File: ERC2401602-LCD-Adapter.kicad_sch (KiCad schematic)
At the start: 27 parts, among them J1 LCD ERC240160XX-2, J2 Backlight, J3 LCD Debug, J4 Backlight Debug, J5 Left, J6 Bottom, Q1 2N7002

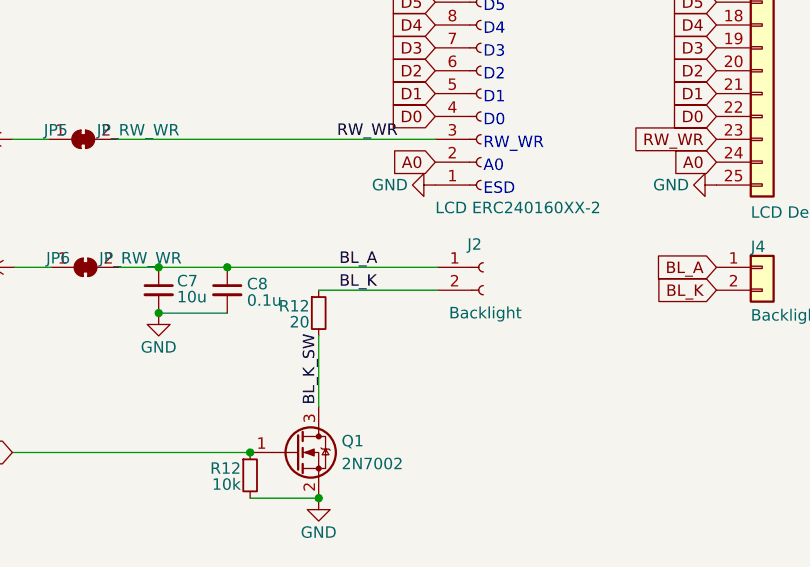
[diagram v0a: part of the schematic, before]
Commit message: Fixed Resistor and BG Polarity
- Changed the current limiting resistor value to 3.9R
- Fixed the Background Light connector Polarity
- Moved the LCD connector down 5mm
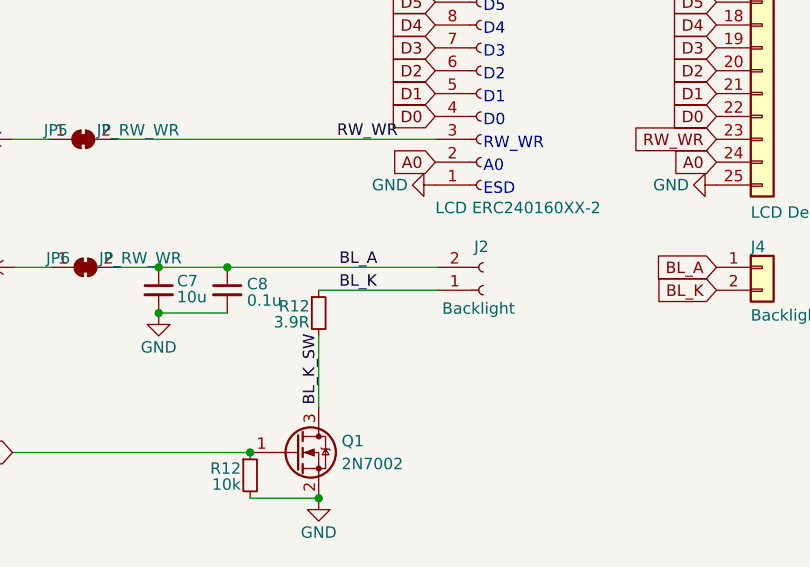
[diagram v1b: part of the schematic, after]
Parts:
- R12: value 20 -> 3.9R; LCSC (none) -> C2907146
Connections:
- net BL_A: now also J2.2 (Pin_2); no longer J2.1 (Pin_1)
- net BL_K: now also J2.1 (Pin_1); no longer J2.2 (Pin_2)
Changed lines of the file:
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@@
       (effects (font (size 1.27 1.27)) (justify right))
     )
-    (property "Value" "20" (at 212.852 106.426 0)
+    (property "Value" "3.9R" (at 212.852 106.426 0)
       (effects (font (size 1.27 1.27)) (justify right))
     )
@@
       (effects (font (size 1.27 1.27)) hide)
     )
-    (property "LCSC" "" (at 213.868 105.41 0)
-      (effects (font (size 1.27 1.27)) hide)
-    )
-    (property "Field5" "" (at 213.868 105.41 0)
+    (property "LCSC" "C2907146" (at 213.868 105.41 0)
       (effects (font (size 1.27 1.27)) hide)
     )
@@
     )
   )
-  (symbol (lib_id "Connector:Conn_01x02_Socket") (at 232.156 100.33 0) (unit 1)
-    (in_bom yes) (on_board yes) (dnp no)
-    (property "Reference" "J2" (at 230.378 97.79 0)
-      (effects (font (size 1.27 1.27)) (justify left))
-    )
-    (property "Value" "Backlight" (at 228.346 105.41 0)
-      (effects (font (size 1.27 1.27)) (justify left))
-    )
-    (property "Footprint" "Connector_JST:JST_PH_S2B-PH-SM4-TB_1x02-1MP_P2.00mm_Horizontal" (at 232.156 100.33 0)
-      (effects (font (size 1.27 1.27)) hide)
-    )
-    (property "Datasheet" "https://jlcpcb.com/partdetail/Jst-S2B_PH_SM4_TB_LF_SN/C295747" (at 232.156 100.33 0)
-      (effects (font (size 1.27 1.27)) hide)
-    )
-    (property "LCSC" "C295747" (at 232.156 100.33 0)
-      (effects (font (size 1.27 1.27)) hide)
-    )
+  (symbol (lib_id "Connector:Conn_01x02_Socket") (at 232.156 102.87 0) (mirror x) (unit 1)
+    (in_bom yes) (on_board yes) (dnp no)
+    (property "Reference" "J2" (at 231.14 98.044 0)
+      (effects (font (size 1.27 1.27)) (justify left))
+    )
+    (property "Value" "Backlight" (at 227.584 104.902 0)
+      (effects (font (size 1.27 1.27)) (justify left))
+    )
+    (property "Footprint" "Connector_JST:JST_PH_S2B-PH-SM4-TB_1x02-1MP_P2.00mm_Horizontal" (at 232.156 102.87 0)
+      (effects (font (size 1.27 1.27)) hide)
+    )
+    (property "Datasheet" "https://jlcpcb.com/partdetail/Jst-S2B_PH_SM4_TB_LF_SN/C295747" (at 232.156 102.87 0)
+      (effects (font (size 1.27 1.27)) hide)
+    )
+    (property "LCSC" "C295747" (at 232.156 102.87 0)
+      (effects (font (size 1.27 1.27)) hide)
+    )

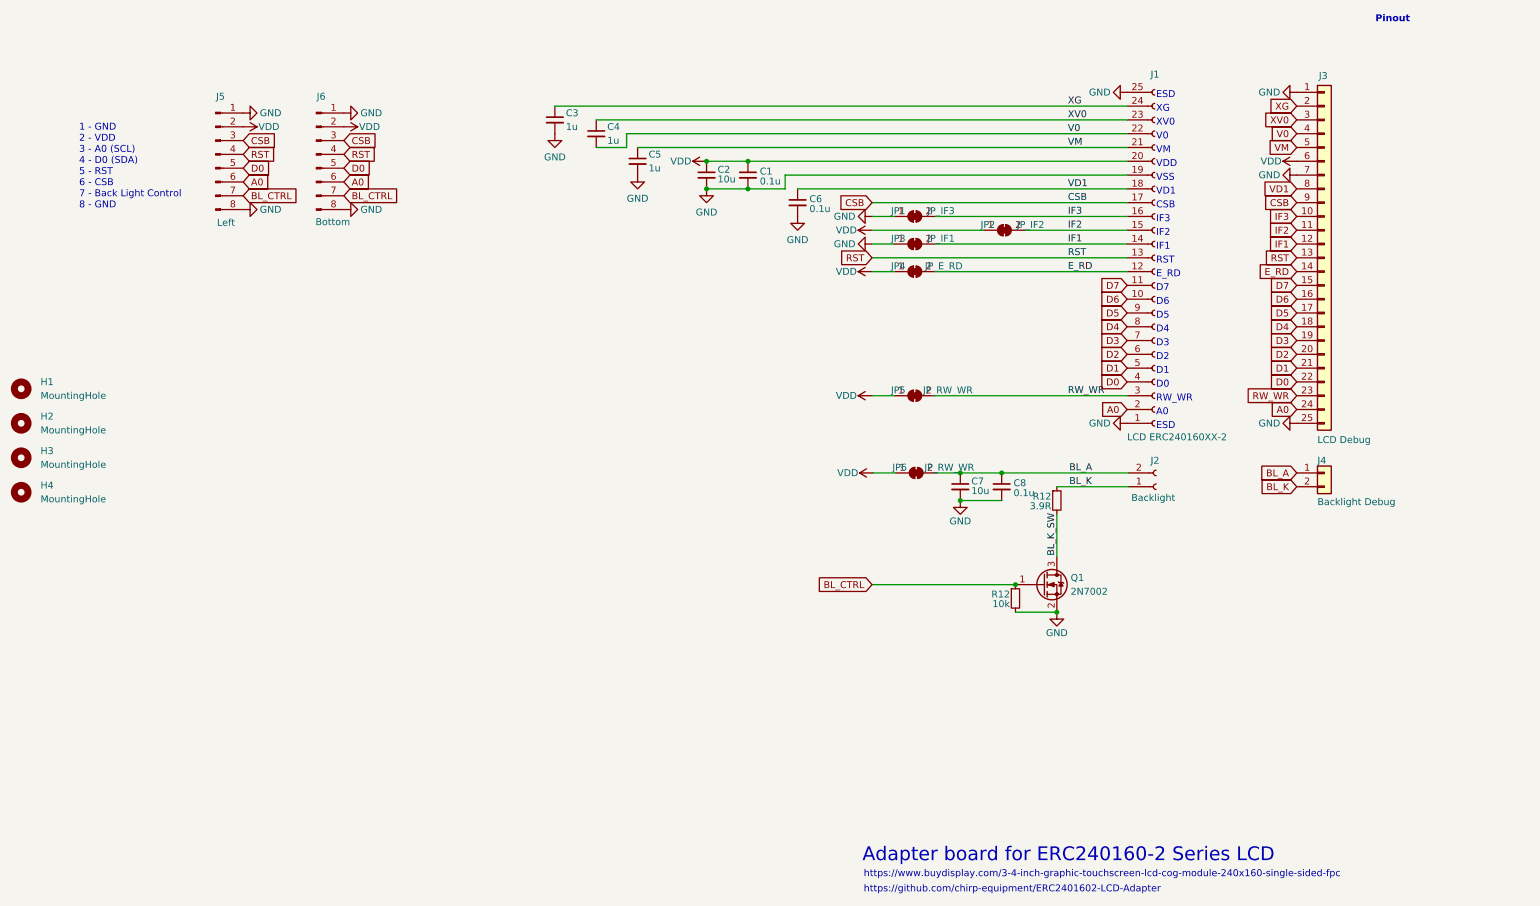
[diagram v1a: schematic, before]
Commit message: Added DC PIN
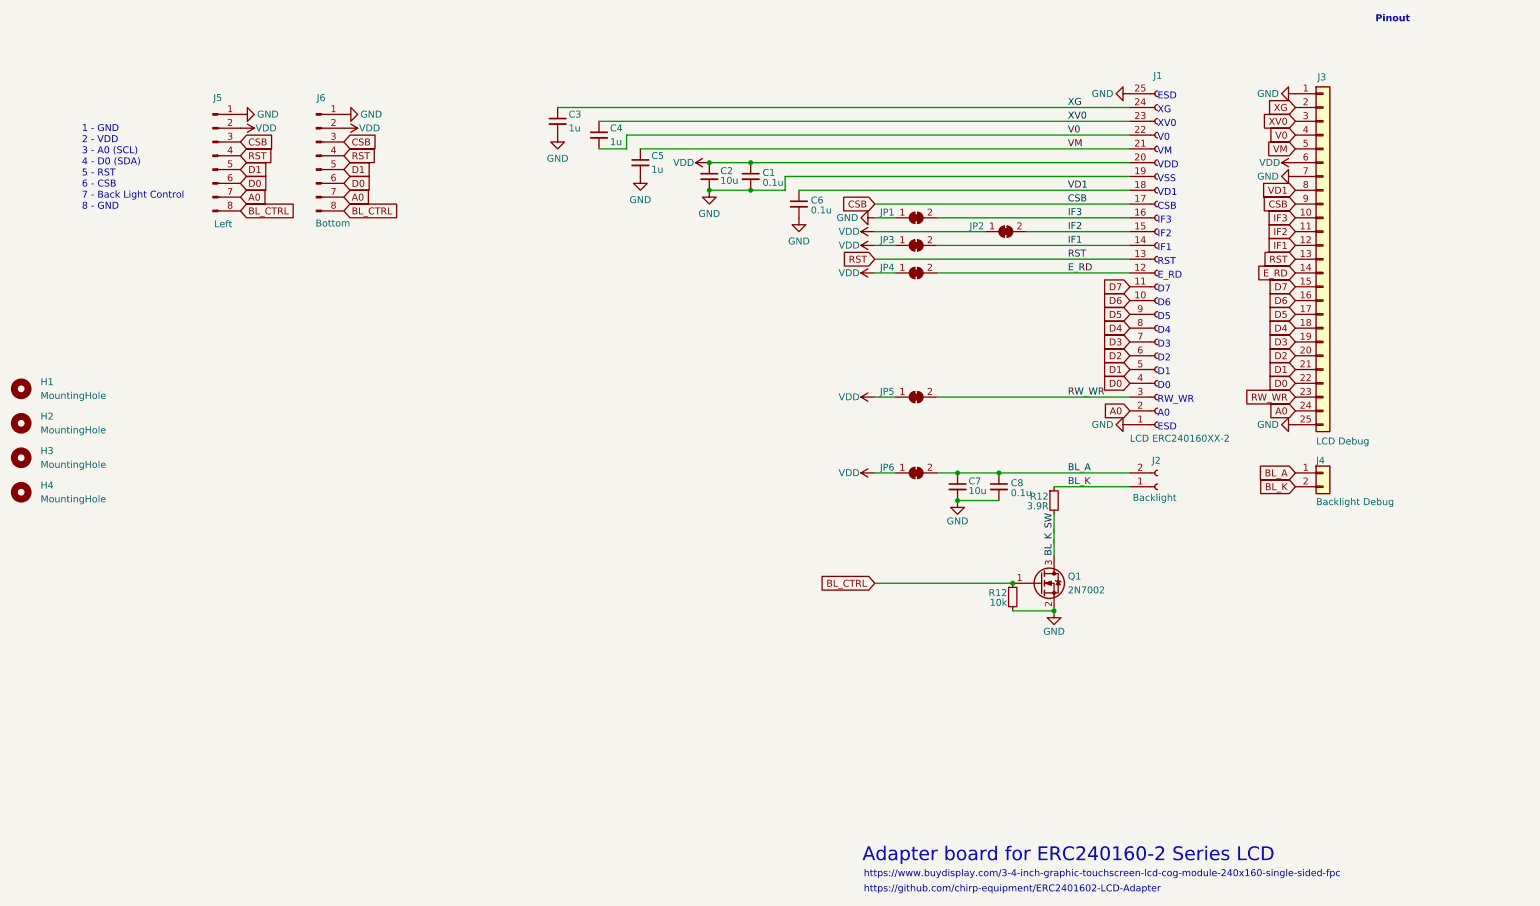
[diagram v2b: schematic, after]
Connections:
- net A0: now also J5.7 (Pin_7), J6.7 (Pin_7); no longer J5.6 (Pin_6), J6.6 (Pin_6)
- net BL_CTRL: now also J5.8 (Pin_8), J6.8 (Pin_8); no longer J5.7 (Pin_7), J6.7 (Pin_7)
- net D0: now also J5.6 (Pin_6), J6.6 (Pin_6); no longer J5.5 (Pin_5), J6.5 (Pin_5)
- net D1: now also J5.5 (Pin_5), J6.5 (Pin_5)
- net GND: no longer J5.8 (Pin_8), J6.8 (Pin_8), JP3.1 (A)
- net VDD: now also JP3.1 (A)
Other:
- moved on the sheet: C1, C2, C3, C4, C5, C7, C8, J1, J5, Q1, R12
